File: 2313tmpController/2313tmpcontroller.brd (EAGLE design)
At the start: 60.6 x 54.6 mm, 32 parts, among them IC1 AT90S2313P, T1 BD139, T2 BD139, T3 BD139, T4 BD139

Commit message: fixed some pads
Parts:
- GNDIN, RSTBTN, VCCIN: device pinhead:1X01 -> wirepad:2,54/0,8
- moved RSTBTN 11.5 mm to (40.6, 68.6)
- moved GNDIN 1.27 mm to (69.8, 19.1)
- moved VCCIN 1.27 mm to (69.8, 68.6)
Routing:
- net N$19: track 14.0 -> 21.6 mm
- net N$9: track 16.5 -> 19.0 mm
- net GND: track 59.7 -> 61.0 mm
- net VCC: track 38.1 -> 39.4 mm
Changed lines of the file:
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@@
 <wire x1="72.06" y1="71.11" x2="11.43" y2="71.11" width="0" layer="20"/>
 <wire x1="11.43" y1="71.11" x2="11.43" y2="16.51" width="0" layer="20"/>
+<circle x="29.21" y="57.15" radius="0.762" width="0.4064" layer="16"/>
+<circle x="36.83" y="57.15" radius="0.762" width="0.4064" layer="16"/>
+<circle x="36.83" y="53.34" radius="0.762" width="0.4064" layer="16"/>
+<circle x="29.21" y="53.34" radius="0.762" width="0.4064" layer="16"/>
+<circle x="29.21" y="49.53" radius="0.762" width="0.4064" layer="16"/>
+<circle x="36.83" y="49.53" radius="0.762" width="0.4064" layer="16"/>
+<circle x="36.83" y="45.72" radius="0.762" width="0.4064" layer="16"/>
+<circle x="29.21" y="45.72" radius="0.762" width="0.4064" layer="16"/>
+<circle x="50.8" y="62.23" radius="0.762" width="0.4064" layer="16"/>
+<circle x="58.42" y="62.23" radius="0.762" width="0.4064" layer="16"/>
+<circle x="62.23" y="62.23" radius="0.762" width="0.4064" layer="16"/>
+<circle x="69.85" y="62.23" radius="0.762" width="0.4064" layer="16"/>
 </plain>
 <attributes>
@@
 <element name="R4" library="rcl" package="0207/7" value="" x="33.02" y="57.15"/>
 <element name="R5" library="rcl" package="0207/7" value="" x="54.61" y="62.23"/>
-<element name="RSTBTN" library="pinhead" package="1X01" value="" x="41.91" y="57.15"/>
 <element name="T1" library="transistor" package="TO126" value="BD139" x="20.32" y="30.48" rot="R90"/>
 <element name="T2" library="transistor" package="TO126" value="BD139" x="20.32" y="40.64" rot="R90"/>
@@
 <element name="T4" library="transistor" package="TO126" value="BD139" x="20.32" y="62.23" rot="R90"/>
 <element name="VCC" library="pinhead" package="1X08" value="" x="54.61" y="68.58" rot="R180"/>
-<element name="VCCIN" library="pinhead" package="1X01" value="" x="68.58" y="68.58"/>
-<element name="GNDIN" library="pinhead" package="1X01" value="" x="68.58" y="19.05"/>
 <element name="PAD1" library="wirepad" package="2,15/1,0" value="WIREPAD2,15/1,0" x="67.31" y="30.48"/>
 <element name="PAD2" library="wirepad" package="2,15/1,0" value="WIREPAD2,15/1,0" x="41.91" y="30.48"/>
@@
 <element name="R6" library="rcl" package="0207/7" value="" x="66.04" y="62.23" rot="R180"/>
 <element name="LED1" library="led" package="Q62902-B153" value="" x="69.85" y="25.4" rot="R90"/>
+<element name="VCCIN" library="wirepad" package="2,54/0,8" value="" x="69.85" y="68.58"/>
+<element name="GNDIN" library="wirepad" package="2,54/0,8" value="" x="69.85" y="19.05"/>
+<element name="RSTBTN" library="wirepad" package="2,54/0,8" value="" x="40.64" y="68.58"/>
 </elements>
 <signals>
@@
 <contactref element="VCC" pad="8"/>
 <contactref element="R5" pad="2"/>
-<contactref element="VCCIN" pad="1"/>
 <wire x1="58.42" y1="62.23" x2="58.42" y2="57.15" width="0.6096" layer="16"/>
 <wire x1="58.42" y1="62.23" x2="58.42" y2="68.58" width="0.6096" layer="16"/>
-<wire x1="68.58" y1="68.58" x2="63.5" y2="68.58" width="0.6096" layer="16"/>
 <wire x1="63.5" y1="68.58" x2="60.96" y2="68.58" width="0.6096" layer="16"/>
 <wire x1="60.96" y1="68.58" x2="58.42" y2="68.58" width="0.6096" layer="16"/>
@@
 <contactref element="R6" pad="2"/>
 <wire x1="62.23" y1="62.23" x2="58.42" y2="62.23" width="0.4064" layer="16"/>
+<contactref element="VCCIN" pad="1"/>
+<wire x1="69.85" y1="68.58" x2="63.5" y2="68.58" width="0.4064" layer="16"/>
 </signal>
 <signal name="GND">
@@
 <contactref element="GND" pad="2"/>
 <contactref element="GND" pad="1"/>
-<contactref element="GNDIN" pad="1"/>
 <wire x1="50.8" y1="34.29" x2="45.72" y2="34.29" width="0.6096" layer="16"/>
 <wire x1="45.72" y1="34.29" x2="45.72" y2="26.67" width="0.6096" layer="16"/>
@@
 <wire x1="43.18" y1="26.67" x2="45.72" y2="26.67" width="0.6096" layer="16"/>
 <wire x1="63.5" y1="19.05" x2="63.5" y2="24.13" width="0.6096" layer="16"/>
-<wire x1="68.58" y1="19.05" x2="63.5" y2="19.05" width="0.6096" layer="16"/>
 <wire x1="63.5" y1="19.05" x2="60.96" y2="19.05" width="0.6096" layer="16"/>
 <wire x1="60.96" y1="19.05" x2="58.42" y2="19.05" width="0.6096" layer="16"/>
@@
 <contactref element="LED1" pad="K"/>
 <wire x1="69.85" y1="24.13" x2="63.5" y2="24.13" width="0.4064" layer="16"/>
+<contactref element="GNDIN" pad="1"/>
+<wire x1="69.85" y1="19.05" x2="63.5" y2="19.05" width="0.4064" layer="16"/>
 </signal>
 <signal name="N$1">
@@
 <wire x1="41.91" y1="54.61" x2="39.37" y2="54.61" width="0.6096" layer="16"/>
 <wire x1="39.37" y1="54.61" x2="39.37" y2="57.15" width="0.6096" layer="16"/>
+<wire x1="39.37" y1="57.15" x2="36.83" y2="57.15" width="0.6096" layer="16"/>
 <wire x1="39.37" y1="57.15" x2="36.83" y2="57.15" width="0.6096" layer="16"/>
 </signal>
@@
 <contactref element="IC1" pad="1"/>
 <contactref element="R5" pad="1"/>
+<wire x1="50.8" y1="62.23" x2="50.8" y2="57.15" width="0.6096" layer="16"/>
 <contactref element="RSTBTN" pad="1"/>
-<wire x1="50.8" y1="57.15" x2="41.91" y2="57.15" width="0.6096" layer="16"/>
-<wire x1="50.8" y1="62.23" x2="50.8" y2="57.15" width="0.6096" layer="16"/>
+<wire x1="40.64" y1="68.58" x2="40.64" y2="62.23" width="0.4064" layer="16"/>
+<wire x1="40.64" y1="62.23" x2="50.8" y2="62.23" width="0.4064" layer="16"/>
 </signal>
 <signal name="N$18">

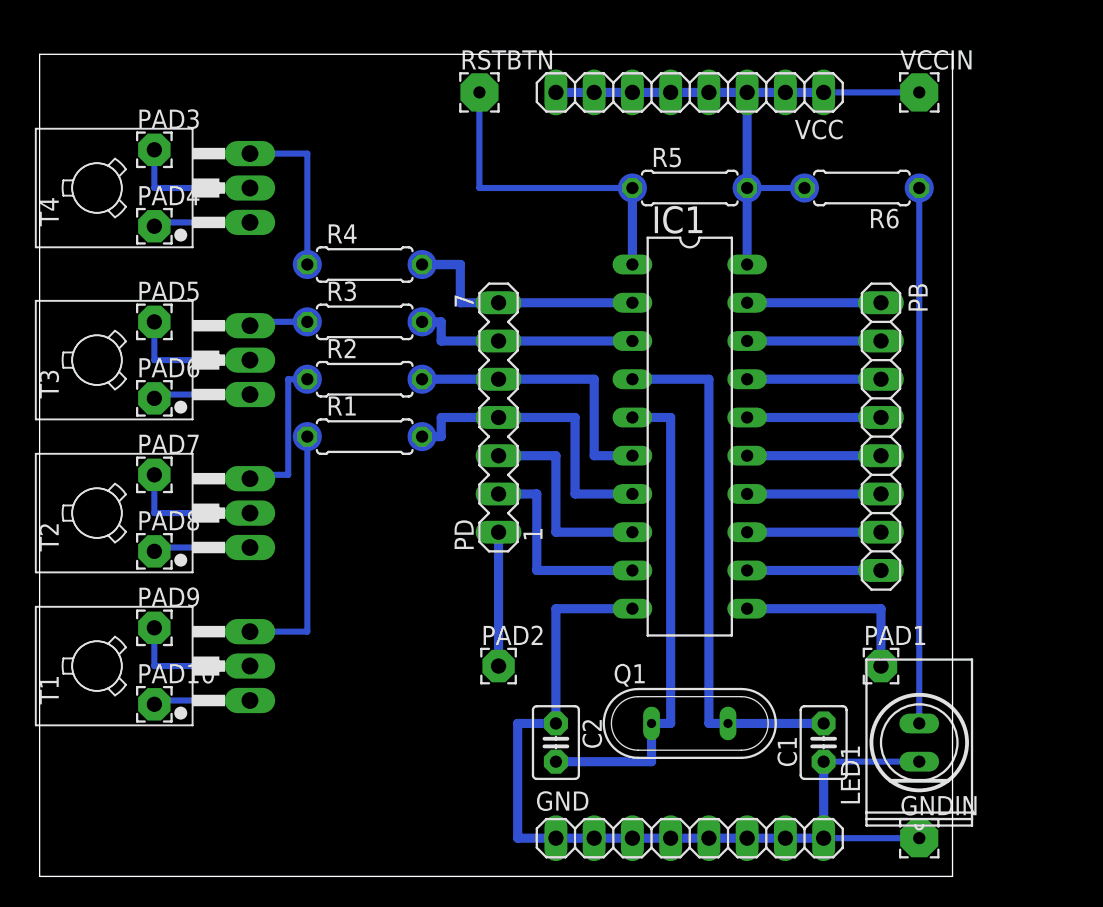
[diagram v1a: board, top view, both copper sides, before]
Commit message: added 7805
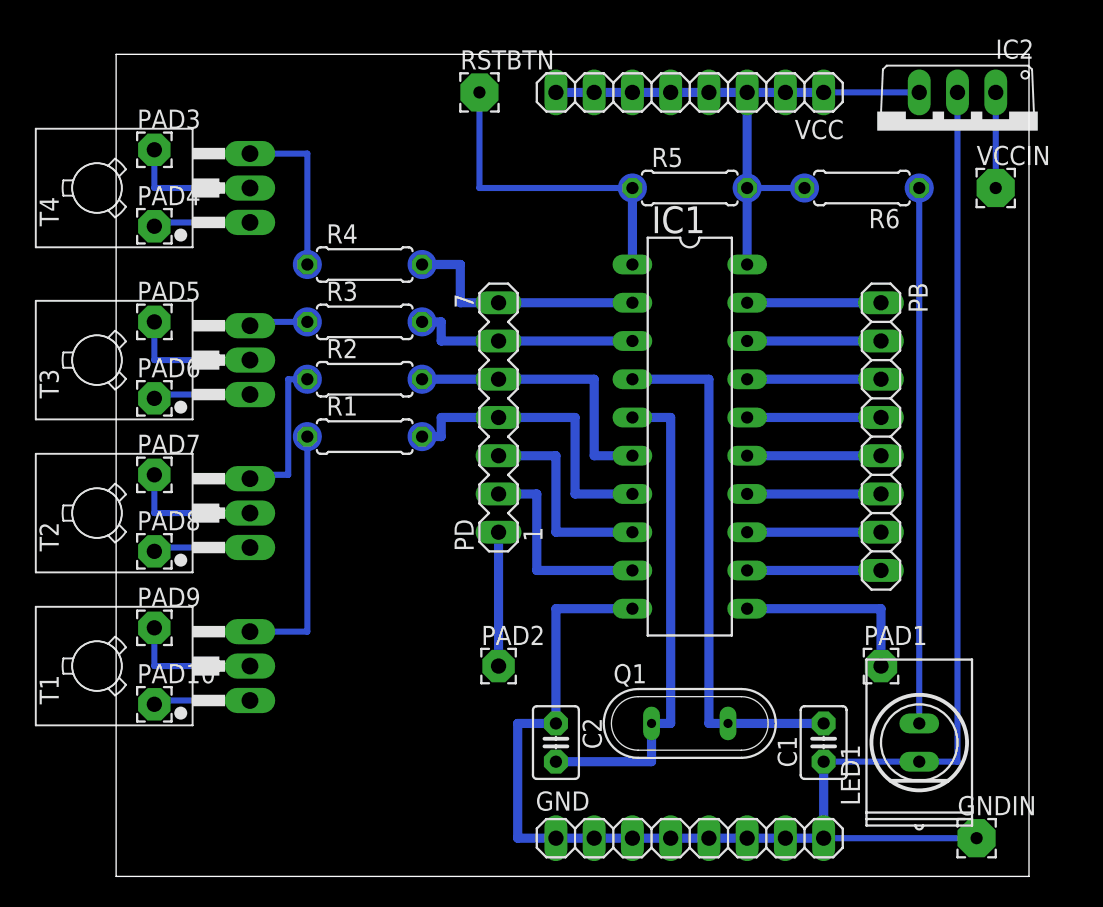
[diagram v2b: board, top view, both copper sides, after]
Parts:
- added IC2: 7805TV, linear:TO220V
- moved VCCIN 8.13 mm to (74.9, 62.2)
- moved GNDIN 3.81 mm to (73.7, 19.1)
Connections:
- new net N$33: IC2.1, VCCIN.1
- net GND: now also IC2.2
- net VCC: now also IC2.3; no longer VCCIN.1
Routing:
- net GND: track 61.0 -> 111.8 mm
- net N$33: track 0.00 -> 6.35 mm
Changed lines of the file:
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@@
 <board>
 <plain>
-<wire x1="11.43" y1="16.51" x2="72.06" y2="16.51" width="0" layer="20"/>
-<wire x1="72.06" y1="16.51" x2="72.06" y2="71.11" width="0" layer="20"/>
-<wire x1="72.06" y1="71.11" x2="11.43" y2="71.11" width="0" layer="20"/>
-<wire x1="11.43" y1="71.11" x2="11.43" y2="16.51" width="0" layer="20"/>
+<wire x1="16.51" y1="16.51" x2="77.14" y2="16.51" width="0" layer="20"/>
+<wire x1="77.14" y1="16.51" x2="77.14" y2="71.11" width="0" layer="20"/>
+<wire x1="77.14" y1="71.11" x2="16.51" y2="71.11" width="0" layer="20"/>
+<wire x1="16.51" y1="71.11" x2="16.51" y2="16.51" width="0" layer="20"/>
 <circle x="29.21" y="57.15" radius="0.762" width="0.4064" layer="16"/>
 <circle x="36.83" y="57.15" radius="0.762" width="0.4064" layer="16"/>
@@
 <element name="R6" library="rcl" package="0207/7" value="" x="66.04" y="62.23" rot="R180"/>
 <element name="LED1" library="led" package="Q62902-B153" value="" x="69.85" y="25.4" rot="R90"/>
-<element name="VCCIN" library="wirepad" package="2,54/0,8" value="" x="69.85" y="68.58"/>
-<element name="GNDIN" library="wirepad" package="2,54/0,8" value="" x="69.85" y="19.05"/>
+<element name="VCCIN" library="wirepad" package="2,54/0,8" value="" x="74.93" y="62.23"/>
+<element name="GNDIN" library="wirepad" package="2,54/0,8" value="" x="73.66" y="19.05"/>
 <element name="RSTBTN" library="wirepad" package="2,54/0,8" value="" x="40.64" y="68.58"/>
+<element name="IC2" library="linear" package="TO220V" value="7805TV" x="72.39" y="66.04" rot="R180"/>
 </elements>
 <signals>
@@
 <contactref element="R6" pad="2"/>
 <wire x1="62.23" y1="62.23" x2="58.42" y2="62.23" width="0.4064" layer="16"/>
-<contactref element="VCCIN" pad="1"/>
+<contactref element="IC2" pad="3"/>
 <wire x1="69.85" y1="68.58" x2="63.5" y2="68.58" width="0.4064" layer="16"/>
 </signal>
@@
 <wire x1="69.85" y1="24.13" x2="63.5" y2="24.13" width="0.4064" layer="16"/>
 <contactref element="GNDIN" pad="1"/>
-<wire x1="69.85" y1="19.05" x2="63.5" y2="19.05" width="0.4064" layer="16"/>
+<wire x1="73.66" y1="19.05" x2="63.5" y2="19.05" width="0.4064" layer="16"/>
+<contactref element="IC2" pad="2"/>
+<wire x1="72.39" y1="68.58" x2="72.39" y2="24.13" width="0.4064" layer="16"/>
+<wire x1="72.39" y1="24.13" x2="69.85" y2="24.13" width="0.4064" layer="16"/>
 </signal>
 <signal name="N$1">
@@
 <wire x1="69.85" y1="26.67" x2="69.85" y2="62.23" width="0.4064" layer="16"/>
 </signal>
+<signal name="N$33">
+<contactref element="IC2" pad="1"/>
+<contactref element="VCCIN" pad="1"/>
+<wire x1="74.93" y1="62.23" x2="74.93" y2="68.58" width="0.4064" layer="16"/>
+</signal>
 </signals>
